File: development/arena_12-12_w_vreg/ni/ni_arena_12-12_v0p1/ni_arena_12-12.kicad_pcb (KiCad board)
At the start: 4 copper layers, 228.6 x 228.6 mm, 126 parts, among them J1 Barrel_Jack, J2 NI_TE_68pos, P1 CONN15, P10 CONN15, P11 CONN15, P12 CONN15, P2 CONN15, P3 CONN15, P4 CONN15, P5 CONN15, P6 CONN15, P7 CONN15, P8 CONN15, P9 CONN15, Q2 MOSFET_NCHAN, SW1 SW_SPDT, U1 TXB0108PW, U10 TPS564201DDC, U11 TPS564201DDC, U12 TPS564201DDC, U13 TPS564201DDC, U14 TPS564201DDC, U15 TPS564201DDC, U16 TPS564201DDC, U17 TPS564201DDC, U18 AP2112K-3.3, U2 TXB0108PW, U3 TXB0108PW, U4 TXB0108PW, U5 TXB0108PW, U6 TPS564201DDC, U7 TPS564201DDC, U8 TPS564201DDC, U9 TPS564201DDC

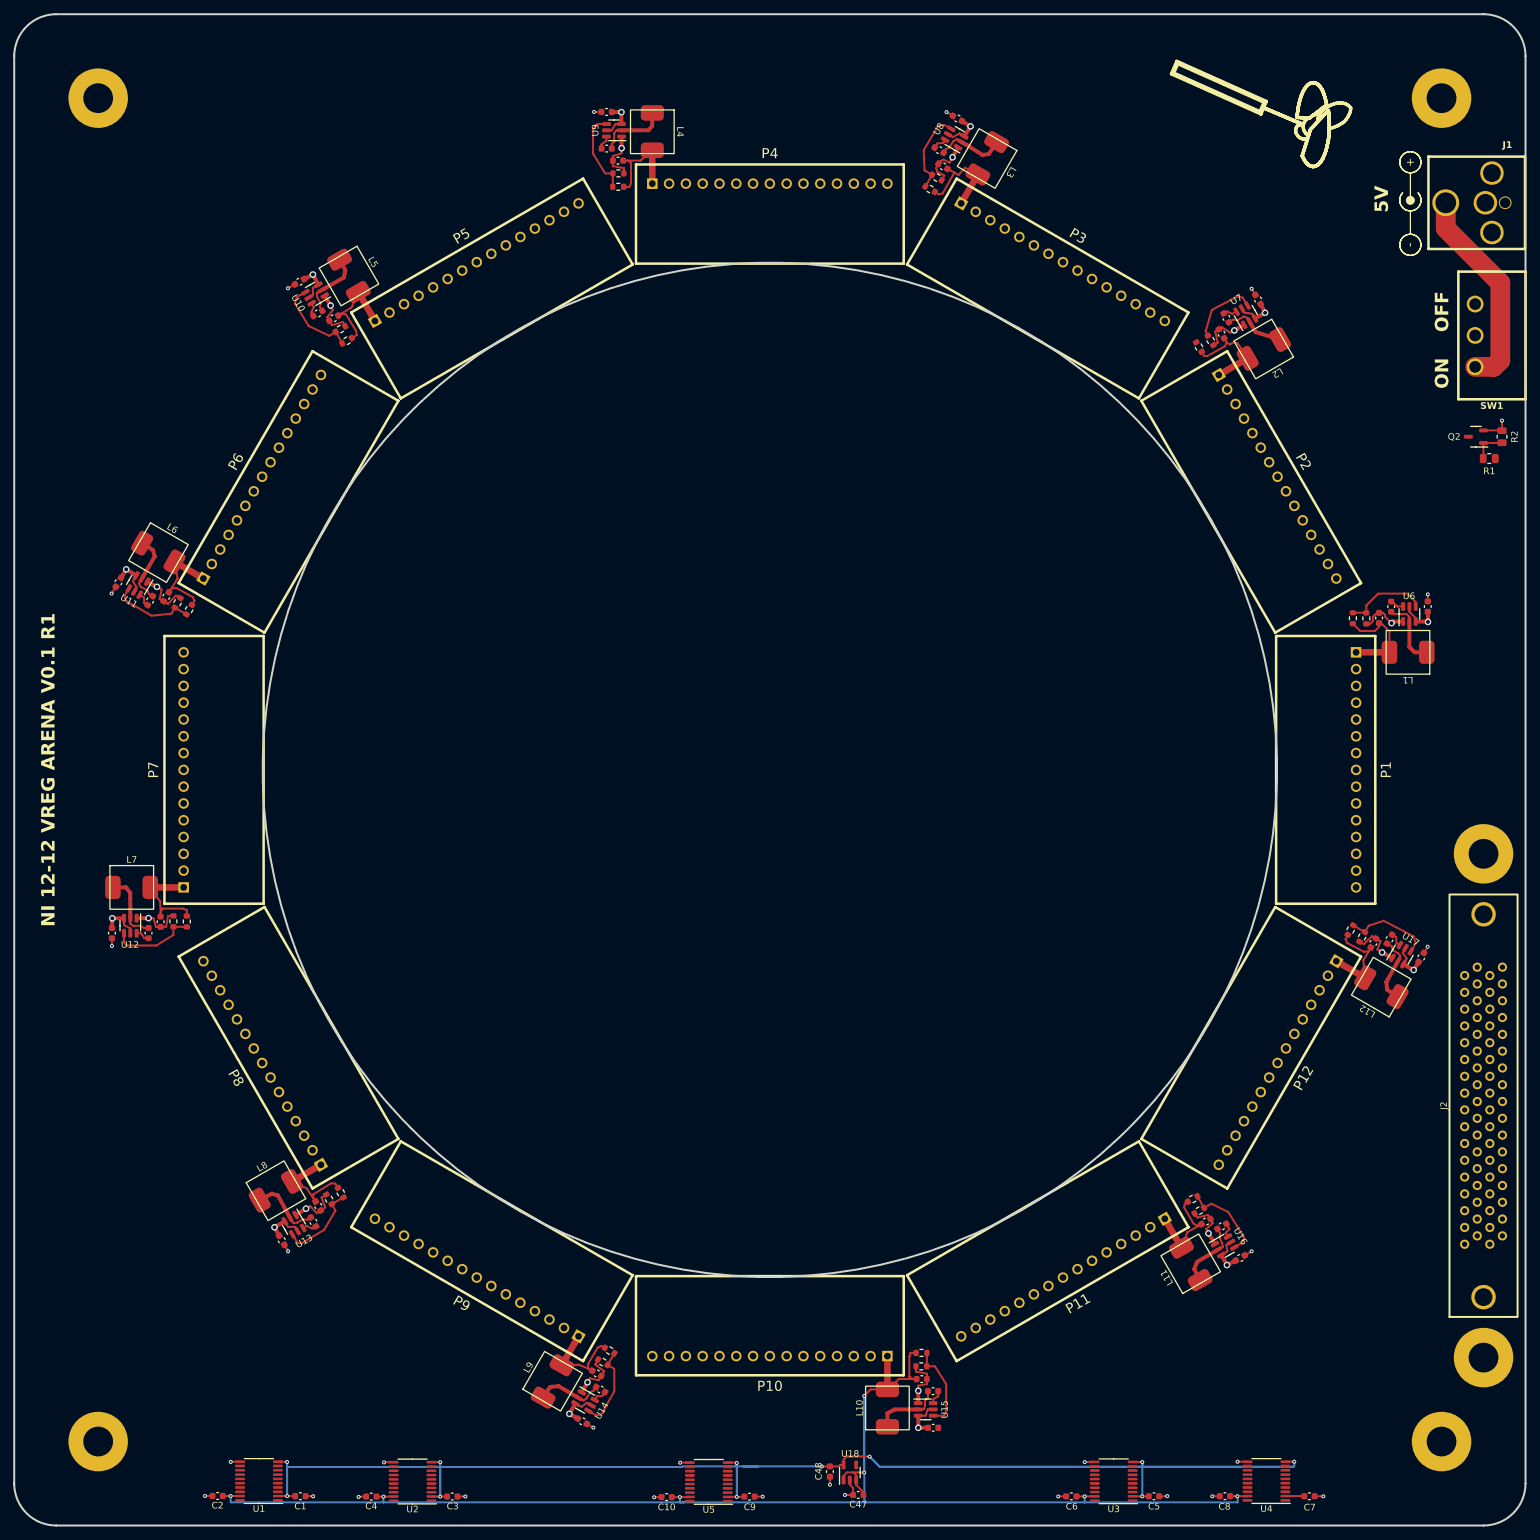
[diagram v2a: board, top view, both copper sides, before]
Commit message: Worked on routing of ni 12-12 arena with vreg.
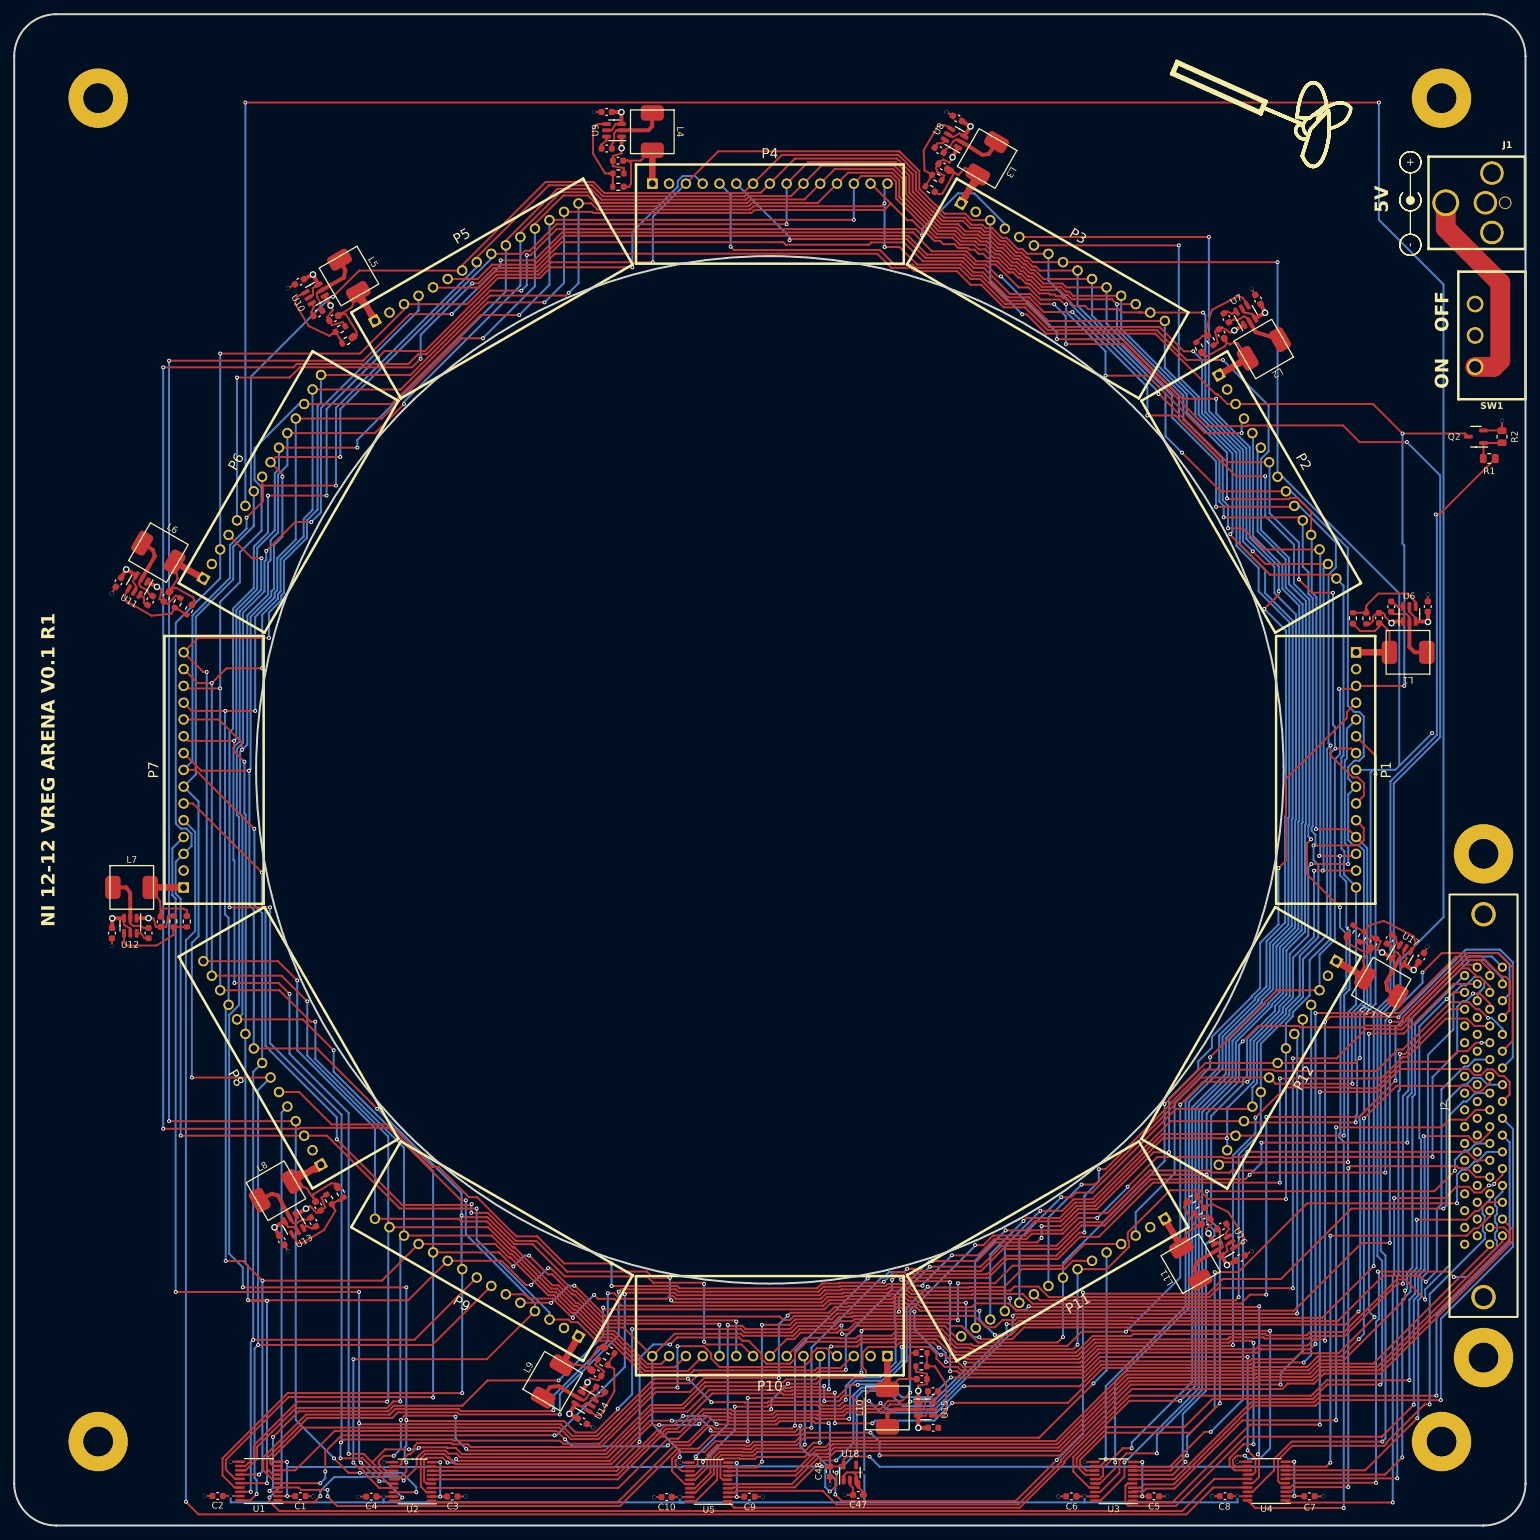
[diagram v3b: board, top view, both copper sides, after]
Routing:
- net /Level Shifters/PAN5V.CS_01: track 0.00 -> 660.3 mm, vias 0 -> 10
- net /Level Shifters/PAN5V.CS_02: track 0.00 -> 653.3 mm, vias 0 -> 12
- net /Level Shifters/PAN5V.CS_03: track 0.00 -> 645.1 mm, vias 0 -> 12
- net /Level Shifters/PAN5V.CS_00: track 0.00 -> 643.9 mm, vias 0 -> 10
- net /Level Shifters/PAN5V.CS_06: track 0.00 -> 642.8 mm, vias 0 -> 11
- net /Level Shifters/PAN5V.CS_04: track 0.00 -> 640.9 mm, vias 0 -> 10
- net /Level Shifters/PAN5V.CS_05: track 0.00 -> 636.6 mm, vias 0 -> 10
- net /Level Shifters/PAN5V.CS_07: track 0.00 -> 636.0 mm, vias 0 -> 11
- net /Panel Headers/RESET: track 0.00 -> 623.8 mm, vias 0 -> 9
- net /Level Shifters/PAN5V.EXT_INT: track 0.00 -> 611.1 mm, vias 0 -> 11
- net /Level Shifters/PAN5V.MISO_05: track 0.00 -> 468.0 mm, vias 0 -> 3
- net /Level Shifters/PAN5V.SCK_01: track 0.00 -> 394.5 mm, vias 0 -> 10
- net /Level Shifters/PAN5V.SCK_02: track 0.00 -> 385.5 mm, vias 0 -> 8
- net /Level Shifters/PAN5V.MOSI_05: track 0.00 -> 382.7 mm, vias 0 -> 9
- net /Level Shifters/PAN5V.SCK_05: track 0.00 -> 371.2 mm, vias 0 -> 11
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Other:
- outline, holes or cut-outs redrawn

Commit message: Fix issues with routed ni 12-12 arena with vreg.
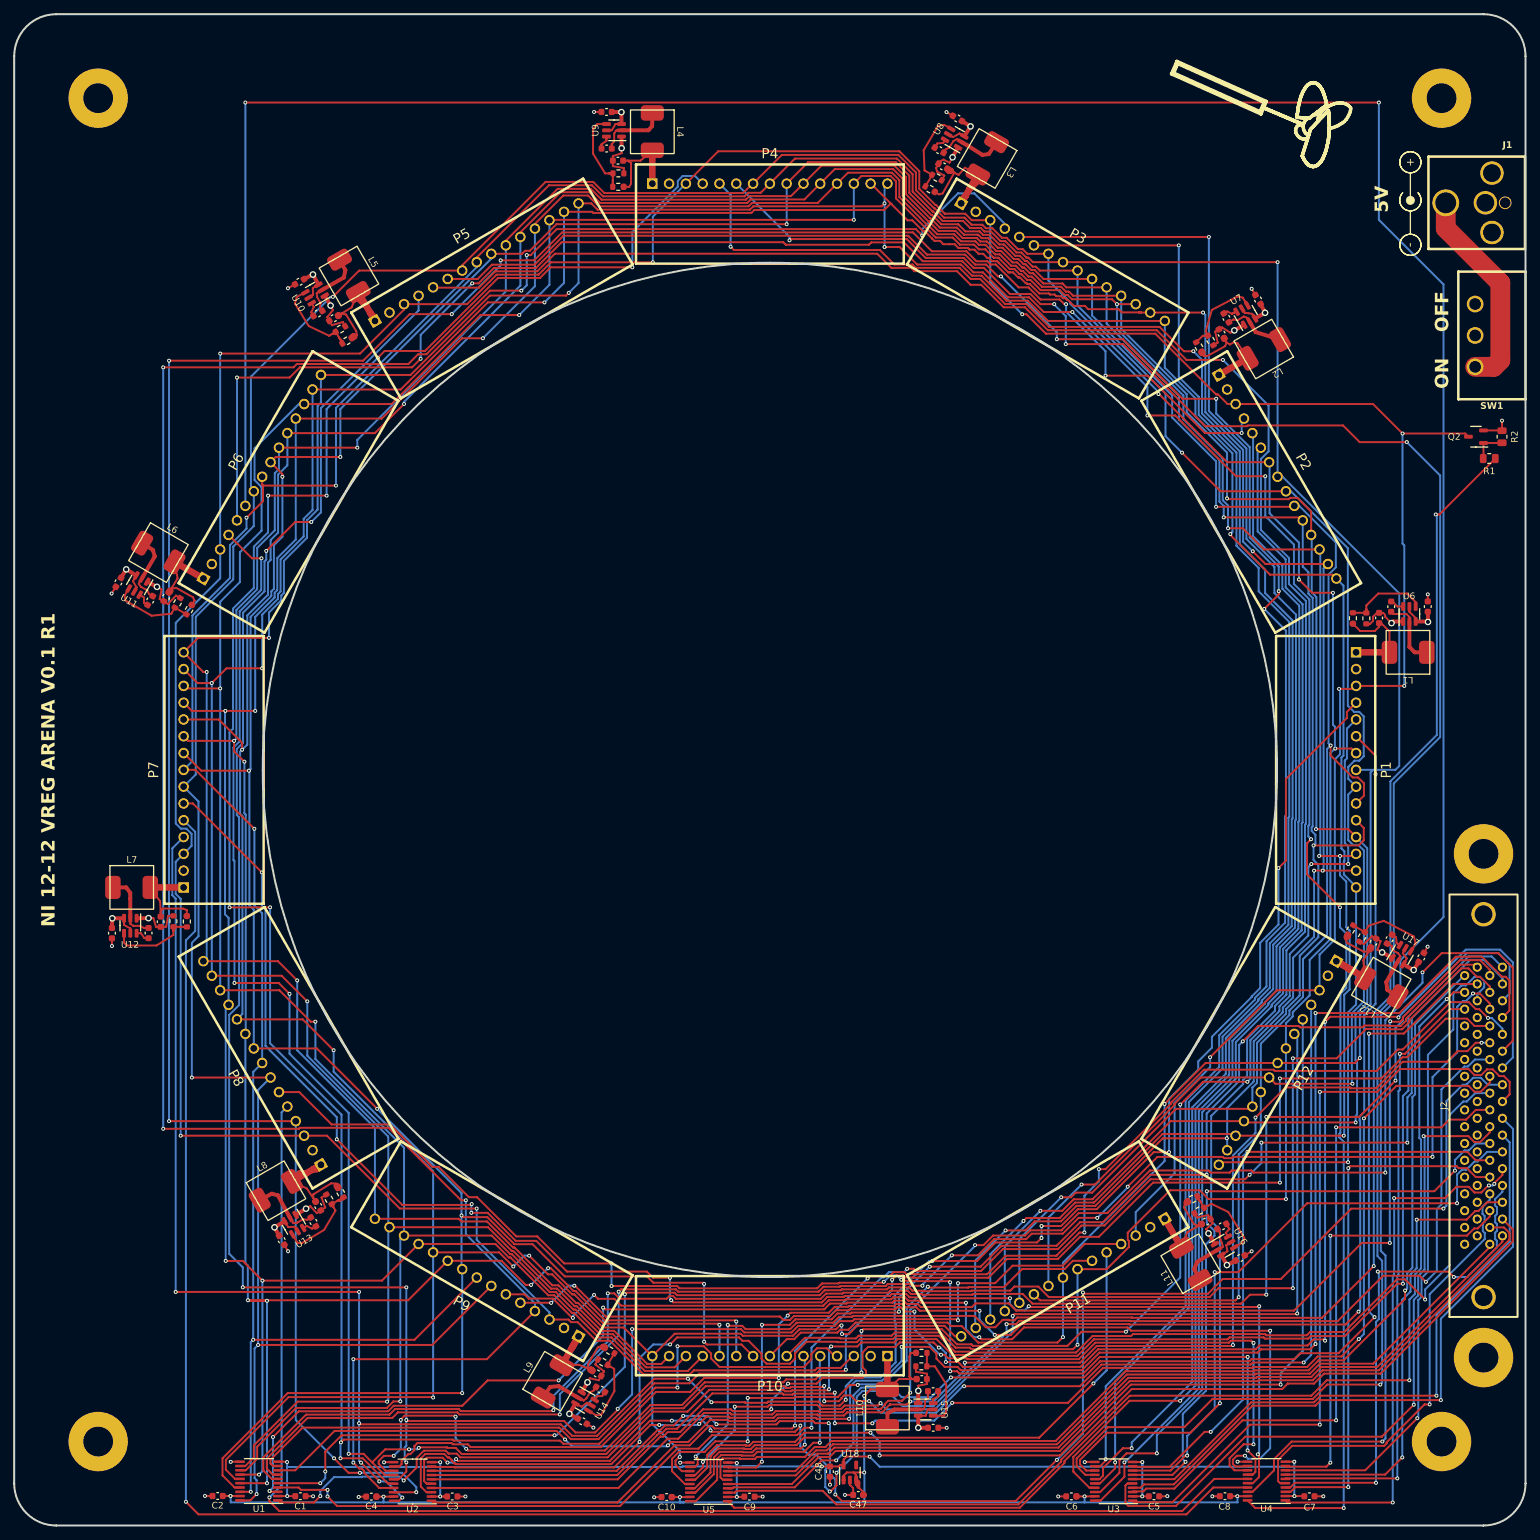
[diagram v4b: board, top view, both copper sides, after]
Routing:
- net /Level Shifters/PAN5V.CS_01: track 660.3 -> 653.2 mm, vias 10 -> 9
- net GND: track 136.0 -> 137.2 mm, vias 41 -> 42
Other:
- outline, holes or cut-outs redrawn
